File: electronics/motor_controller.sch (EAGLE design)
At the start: 45 parts

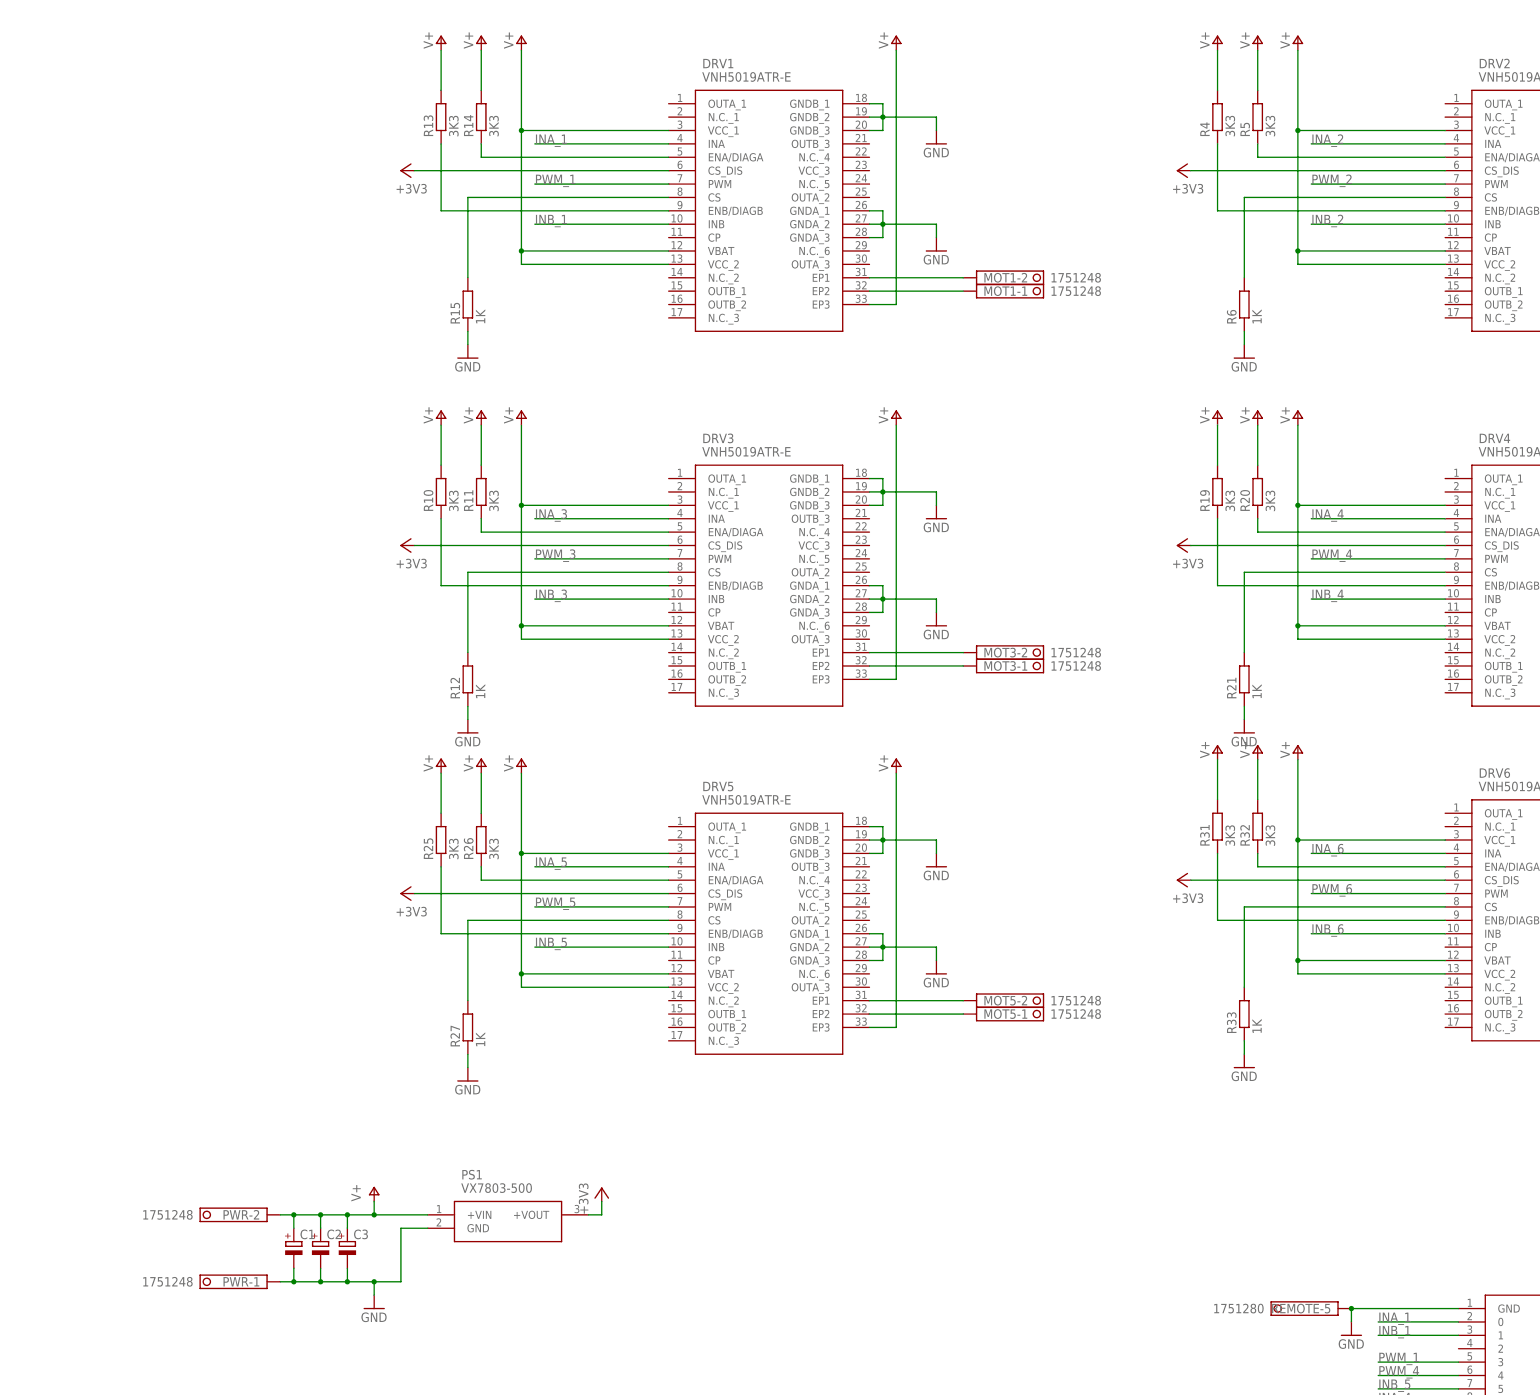
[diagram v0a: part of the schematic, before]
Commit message: Design Review V1
Changed the signal levels from V+ to 3V3 with 3K3 resistors
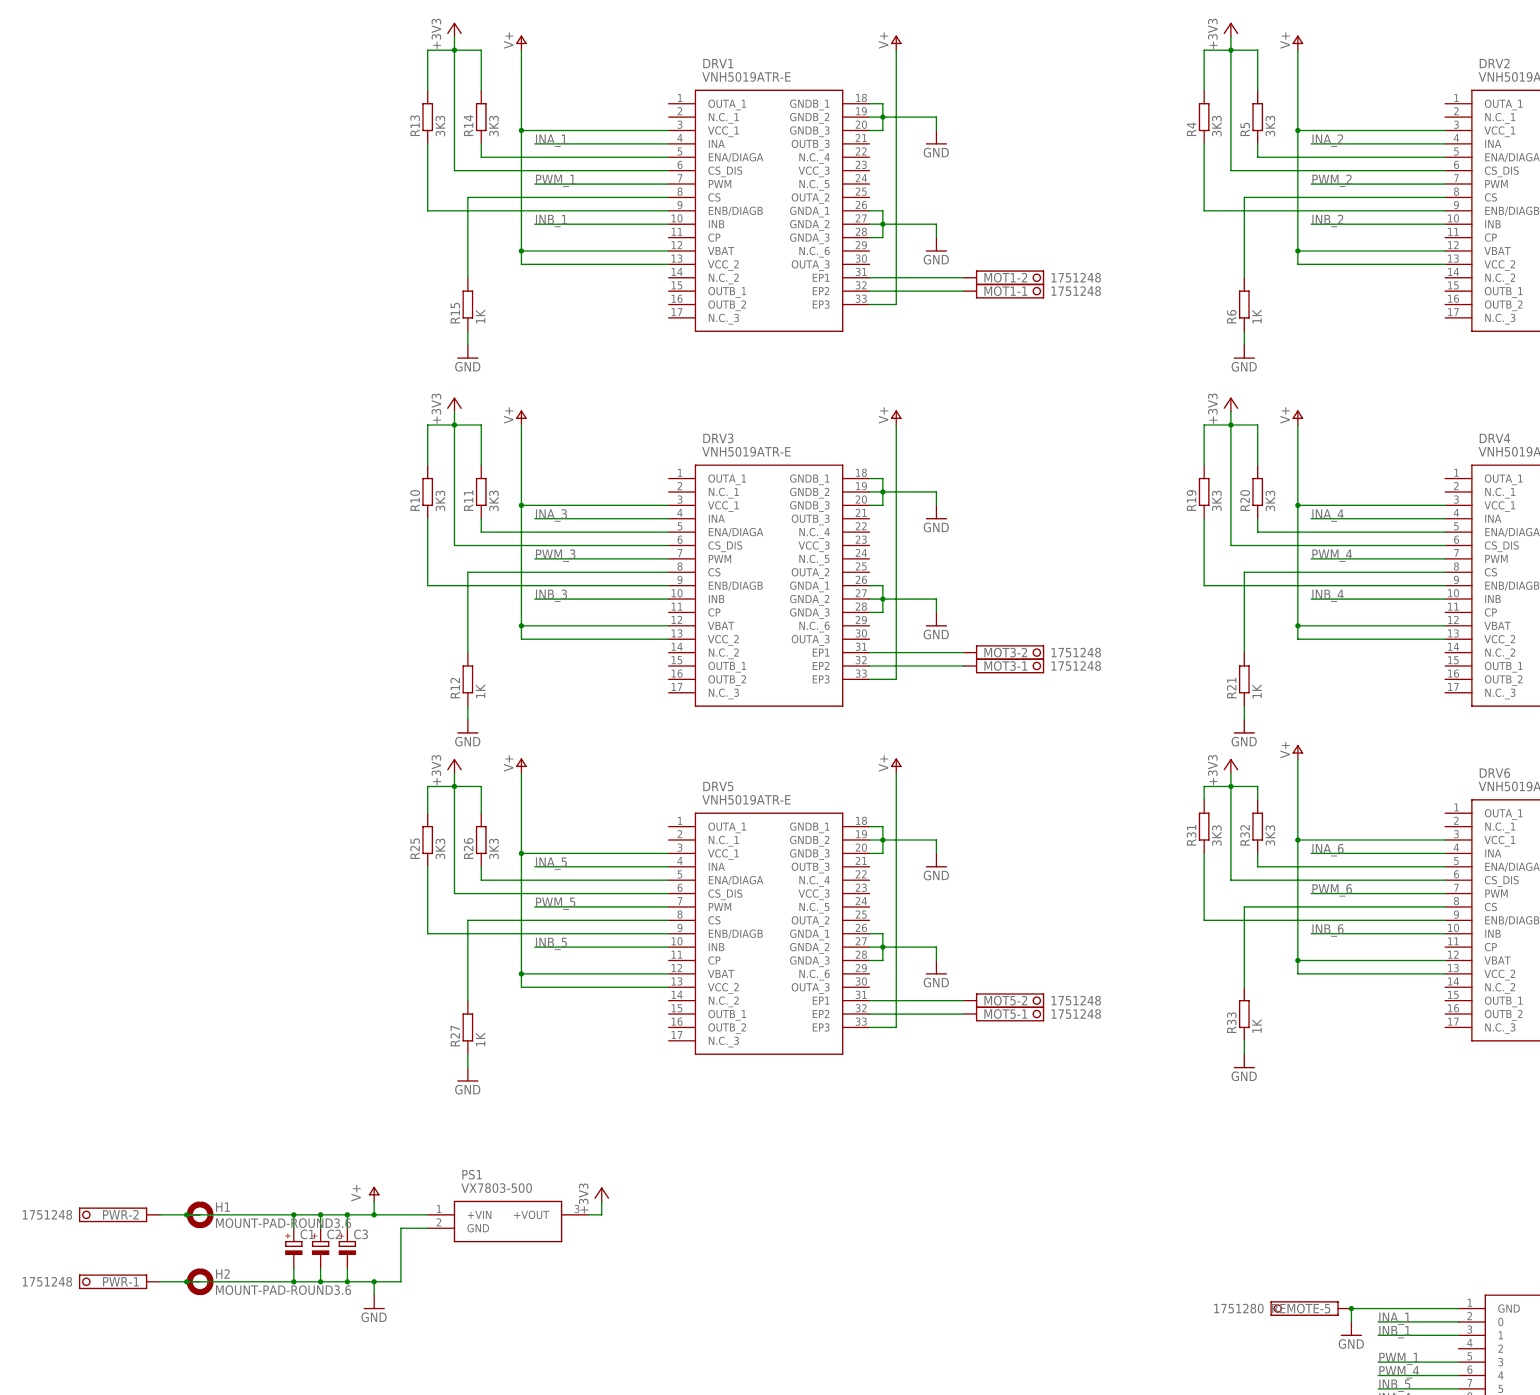
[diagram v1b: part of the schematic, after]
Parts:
- added H1, H2: MOUNT-PAD-ROUND3.6, holes:MOUNT-PAD-ROUND3.6
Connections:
- net +3V3: now also R10.2, R11.2, R13.2, R14.2, R19.2, R20.2, R25.2, R26.2, R31.2, R32.2, R4.2, R5.2
- net GND: now also H2.MOUNT
- net V+: now also H1.MOUNT; no longer R10.2, R11.2, R13.2, R14.2, R19.2, R20.2, R25.2, R26.2, R31.2, R32.2, R4.2, R5.2
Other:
- moved on the sheet: PWR-1, PWR-2, R10, R13, R19, R25, R31, R4

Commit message: Added digikey to BOM
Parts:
- C4, C5, C6, C7: value (none) -> 10uF
- R1, R2, R3, R7: value (none) -> 10k
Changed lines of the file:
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@@
 <part name="GND3" library="supply1" library_urn="urn:adsk.eagle:library:371" deviceset="GND" device=""/>
 <part name="GND1" library="supply1" library_urn="urn:adsk.eagle:library:371" deviceset="GND" device=""/>
-<part name="C4" library="rcl" library_urn="urn:adsk.eagle:library:334" deviceset="C-EU" device="C0603" package3d_urn="urn:adsk.eagle:package:23616/2"/>
-<part name="C5" library="rcl" library_urn="urn:adsk.eagle:library:334" deviceset="C-EU" device="C0603" package3d_urn="urn:adsk.eagle:package:23616/2"/>
-<part name="C6" library="rcl" library_urn="urn:adsk.eagle:library:334" deviceset="C-EU" device="C0603" package3d_urn="urn:adsk.eagle:package:23616/2"/>
-<part name="C7" library="rcl" library_urn="urn:adsk.eagle:library:334" deviceset="C-EU" device="C0603" package3d_urn="urn:adsk.eagle:package:23616/2"/>
-<part name="R1" library="rcl" library_urn="urn:adsk.eagle:library:334" deviceset="R-EU_" device="R0603" package3d_urn="urn:adsk.eagle:package:23555/2"/>
-<part name="R2" library="rcl" library_urn="urn:adsk.eagle:library:334" deviceset="R-EU_" device="R0603" package3d_urn="urn:adsk.eagle:package:23555/2"/>
-<part name="R3" library="rcl" library_urn="urn:adsk.eagle:library:334" deviceset="R-EU_" device="R0603" package3d_urn="urn:adsk.eagle:package:23555/2"/>
-<part name="R7" library="rcl" library_urn="urn:adsk.eagle:library:334" deviceset="R-EU_" device="R0603" package3d_urn="urn:adsk.eagle:package:23555/2"/>
+<part name="C4" library="rcl" library_urn="urn:adsk.eagle:library:334" deviceset="C-EU" device="C0603" package3d_urn="urn:adsk.eagle:package:23616/2" value="10uF"/>
+<part name="C5" library="rcl" library_urn="urn:adsk.eagle:library:334" deviceset="C-EU" device="C0603" package3d_urn="urn:adsk.eagle:package:23616/2" value="10uF"/>
+<part name="C6" library="rcl" library_urn="urn:adsk.eagle:library:334" deviceset="C-EU" device="C0603" package3d_urn="urn:adsk.eagle:package:23616/2" value="10uF"/>
+<part name="C7" library="rcl" library_urn="urn:adsk.eagle:library:334" deviceset="C-EU" device="C0603" package3d_urn="urn:adsk.eagle:package:23616/2" value="10uF"/>
+<part name="R1" library="rcl" library_urn="urn:adsk.eagle:library:334" deviceset="R-EU_" device="R0603" package3d_urn="urn:adsk.eagle:package:23555/2" value="10k"/>
+<part name="R2" library="rcl" library_urn="urn:adsk.eagle:library:334" deviceset="R-EU_" device="R0603" package3d_urn="urn:adsk.eagle:package:23555/2" value="10k"/>
+<part name="R3" library="rcl" library_urn="urn:adsk.eagle:library:334" deviceset="R-EU_" device="R0603" package3d_urn="urn:adsk.eagle:package:23555/2" value="10k"/>
+<part name="R7" library="rcl" library_urn="urn:adsk.eagle:library:334" deviceset="R-EU_" device="R0603" package3d_urn="urn:adsk.eagle:package:23555/2" value="10k"/>
 <part name="H1" library="holes" library_urn="urn:adsk.eagle:library:237" deviceset="MOUNT-PAD-ROUND" device="3.6" package3d_urn="urn:adsk.eagle:package:14284/1" value="MOUNT-PAD-ROUND3.6"/>
 <part name="H2" library="holes" library_urn="urn:adsk.eagle:library:237" deviceset="MOUNT-PAD-ROUND" device="3.6" package3d_urn="urn:adsk.eagle:package:14284/1" value="MOUNT-PAD-ROUND3.6"/>
